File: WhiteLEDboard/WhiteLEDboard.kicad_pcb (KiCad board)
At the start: 2 copper layers, 16.5 x 14 mm, 7 parts, among them J1 CONN_01X02

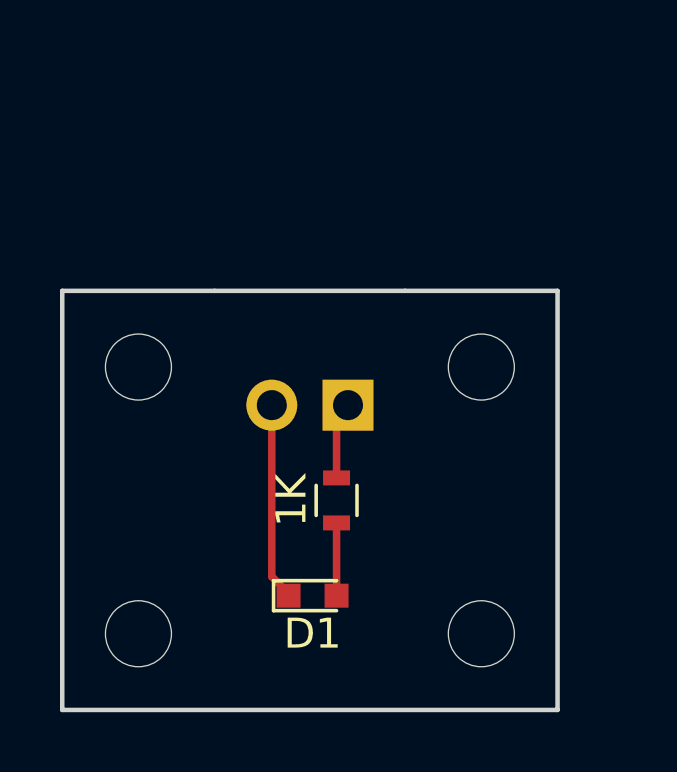
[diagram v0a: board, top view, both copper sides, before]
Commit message: Added WhiteLEDboard
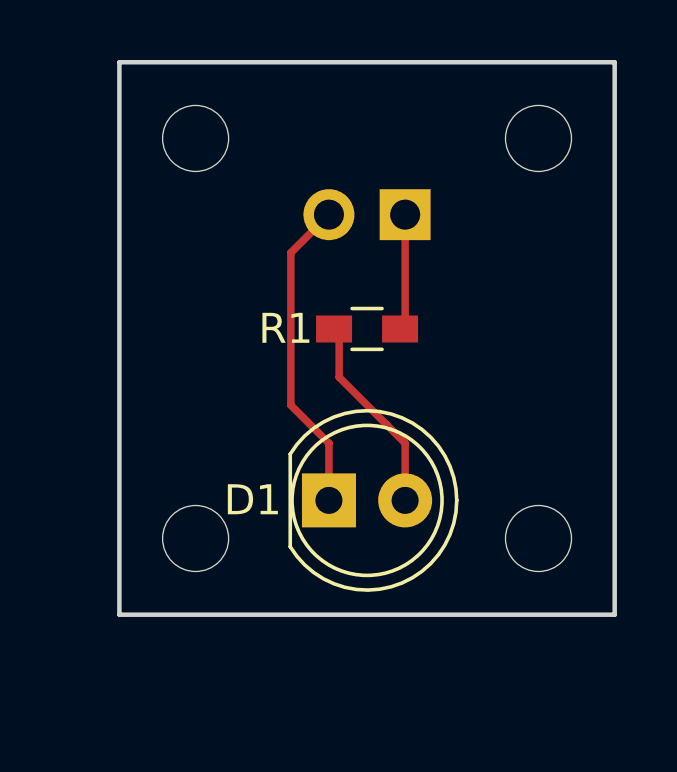
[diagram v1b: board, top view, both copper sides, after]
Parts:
- removed the REF** at (153.7, 110.5)
- removed the REF** at (142.2, 110.5)
- removed the REF** at (142.2, 101.6)
- removed the REF** at (153.7, 101.6)
- added REF**: MountingHole_2.2mm_M2, Mounting_Holes:MountingHole_2.2mm_M2, F.Cu at (155.6, 107.3)
- added REF**: MountingHole_2.2mm_M2, Mounting_Holes:MountingHole_2.2mm_M2, F.Cu at (144.1, 107.3)
- added REF**: MountingHole_2.2mm_M2, Mounting_Holes:MountingHole_2.2mm_M2, F.Cu at (144.1, 94.0)
- added REF**: MountingHole_2.2mm_M2, Mounting_Holes:MountingHole_2.2mm_M2, F.Cu at (155.6, 94.0)
- D1: value SML-D15UW -> LED; footprint LEDs:LED_0603 -> LEDs:LED_D5.0mm
- R1: value 1K -> 10k; footprint Resistors_SMD:R_0603 -> Resistors_SMD:R_0603_HandSoldering
- moved J1 6.63 mm to (151.1, 96.5)
- moved R1 5.80 mm to (149.9, 100.3), turned to 180 degrees
- moved D1 3.22 mm to (148.6, 106.0)
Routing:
- net Net-(D1-Pad2): track 2.42 -> 6.63 mm
- net GND: track 6.58 -> 10.6 mm
- net +5V: track 2.58 -> 3.81 mm
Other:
- board size 16.5 x 14 mm -> 16.5 x 18.4 mm
- board text added: "WhiteLED"
- board text removed: "620nm LED"
